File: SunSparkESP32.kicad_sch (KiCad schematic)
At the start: 50 parts, among them J1 Conn_01x02_Pin, J2 USB_C_Receptacle_USB2.0, J4 Conn_01x15_Pin, J5 Conn_01x03_Pin, J6 Conn_01x15_Pin, J7 Conn_01x01_Pin, Q1 IRLML6244TRPBF, Q2 IRLML6244TRPBF, SW1 SW_Push, SW2 SW_Push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

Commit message: Minor improvements on documentation
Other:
- note added: "Dimensioned as follows: 300µA average current, needs to be supplied for 12h (during night) U(0)=3.5V -> U(12h)=3.1V At least ~32F Powerstage must tolerate 100mA for ~200ms Current spikes 300mA for 1ms R_ESR + R_SYS + R_BAT + R_PGOOD = 0.2 + 0.48 + 0.55 + 0.02 = 1.25Ohm"
- note removed: "Dimensioned as follows: 300µA average current, needs to be supplied for 12h (during night) U(0)=3.5V -> U(12h)=3.1V At least ~32F"
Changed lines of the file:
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@@
     (effects (font (size 1.27 1.27)) (justify left bottom))
   )
-  (text "Dimensioned as follows:\n300µA average current, needs to\nbe supplied for 12h (during night)\nU(0)=3.5V -> U(12h)=3.1V\nAt least ~32F"
-    (at 106.68 52.07 0)
+  (text "Dimensioned as follows:\n300µA average current, needs to\nbe supplied for 12h (during night)\nU(0)=3.5V -> U(12h)=3.1V\nAt least ~32F\n\nPowerstage must tolerate 100mA for ~200ms\nCurrent spikes 300mA for 1ms\nR_ESR + R_SYS + R_BAT + R_PGOOD =\n0.2 + 0.48 + 0.55 + 0.02 = 1.25Ohm"
+    (at 106.68 45.72 0)
     (effects (font (size 1.27 1.27)) (justify left bottom))
   )

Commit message: Final adjustments for release preparation -Updated schematics, BOM and fabrication files -Added solder jumper so RFM96 can be powered independently
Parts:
- added JP2: SolderJumper_2_Open, Jumper:SolderJumper-2_P1.3mm_Open_RoundedPad1.0x1.5mm, symbol Jumper:SolderJumper_2_Open
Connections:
- net +BATT: now also JP2.2 (B); no longer U4.13 (3.3V)
- new net: JP2.1 (A), U4.13 (3.3V)
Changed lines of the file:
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@@
-    (stroke (width 0) (type default))
-  )
-  (wire (pts (xy 223.52 184.15) (xy 223.52 186.69))
     (stroke (width 0) (type default))
   )
@@
     (stroke (width 0) (type default))
   )
+  (wire (pts (xy 223.52 184.785) (xy 223.52 186.69))
+    (stroke (width 0) (type default))
+  )
   (wire (pts (xy 86.36 104.14) (xy 88.9 104.14))
     (stroke (width 0) (type default))
@@
   )
   (wire (pts (xy 82.55 143.51) (xy 91.44 143.51))
+    (stroke (width 0) (type default))
+  )
+  (wire (pts (xy 223.52 173.99) (xy 223.52 177.165))
     (stroke (width 0) (type default))
   )
@@
     )
   )
-  (symbol (lib_id "power:+BATT") (at 223.52 184.15 0) (unit 1)
-    (in_bom yes) (on_board yes) (dnp no) (fields_autoplaced)
-    (property "Reference" "#PWR035" (at 223.52 187.96 0)
-      (effects (font (size 1.27 1.27)) hide)
-    )
-    (property "Value" "+BATT" (at 223.52 180.34 0)
-      (effects (font (size 1.27 1.27)))
-    )
-    (property "Footprint" "" (at 223.52 184.15 0)
-      (effects (font (size 1.27 1.27)) hide)
-    )
-    (property "Datasheet" "" (at 223.52 184.15 0)
+  (symbol (lib_id "power:+BATT") (at 223.52 173.99 0) (unit 1)
+    (in_bom yes) (on_board yes) (dnp no) (fields_autoplaced)
+    (property "Reference" "#PWR035" (at 223.52 177.8 0)
+      (effects (font (size 1.27 1.27)) hide)
+    )
+    (property "Value" "+BATT" (at 223.52 170.18 0)
+      (effects (font (size 1.27 1.27)))
+    )
+    (property "Footprint" "" (at 223.52 173.99 0)
+      (effects (font (size 1.27 1.27)) hide)
+    )
+    (property "Datasheet" "" (at 223.52 173.99 0)
       (effects (font (size 1.27 1.27)) hide)
     )
@@
         )
       )
+    )
+  )
+  (symbol (lib_id "Jumper:SolderJumper_2_Open") (at 223.52 180.975 90) (unit 1)
+    (in_bom yes) (on_board yes) (dnp no) (fields_autoplaced)
+    (property "Reference" "JP2" (at 225.425 180.34 90)
+      (effects (font (size 1.27 1.27)) (justify right))
+    )
+    (property "Value" "SolderJumper_2_Open" (at 225.425 182.88 90)
+      (effects (font (size 1.27 1.27)) (justify right))
+    )
+    (property "Footprint" "Jumper:SolderJumper-2_P1.3mm_Open_RoundedPad1.0x1.5mm" (at 223.52 180.975 0)
+      (effects (font (size 1.27 1.27)) hide)
+    )
+    (property "Datasheet" "~" (at 223.52 180.975 0)
+      (effects (font (size 1.27 1.27)) hide)
+    )
+    (pin "1")
+    (pin "2")
+    (instances
+      (project "SunSparkESP32"
+        (path "/d10941bc-74a1-4d19-894b-f93374d839a2"
+          (reference "JP2") (unit 1)
+        )
+      )

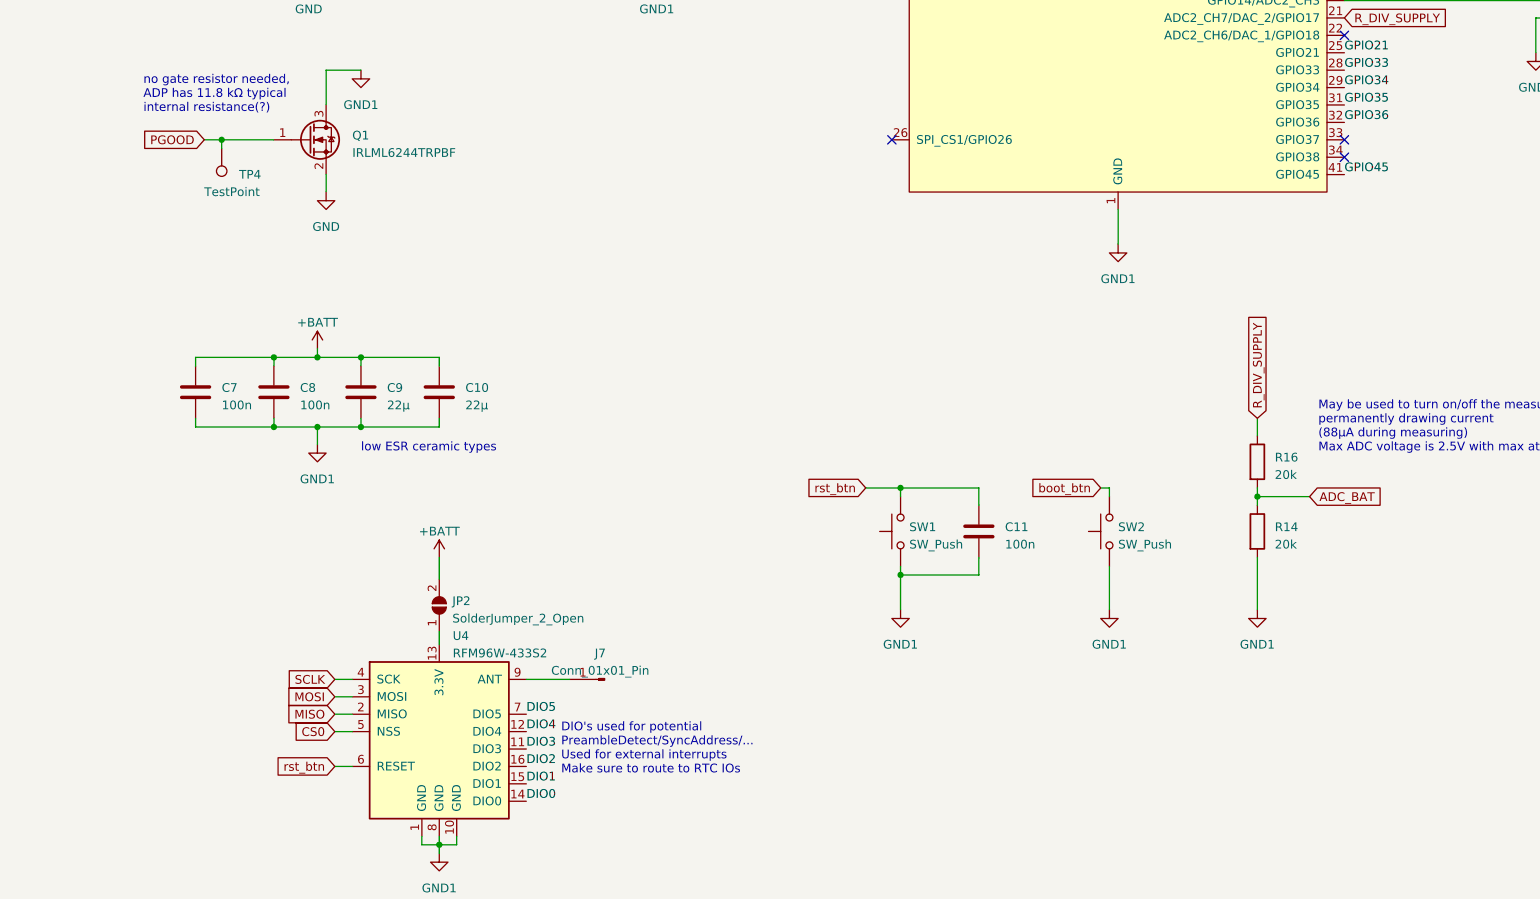
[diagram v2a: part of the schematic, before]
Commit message: connected RF96 pin to µC instead of reset button
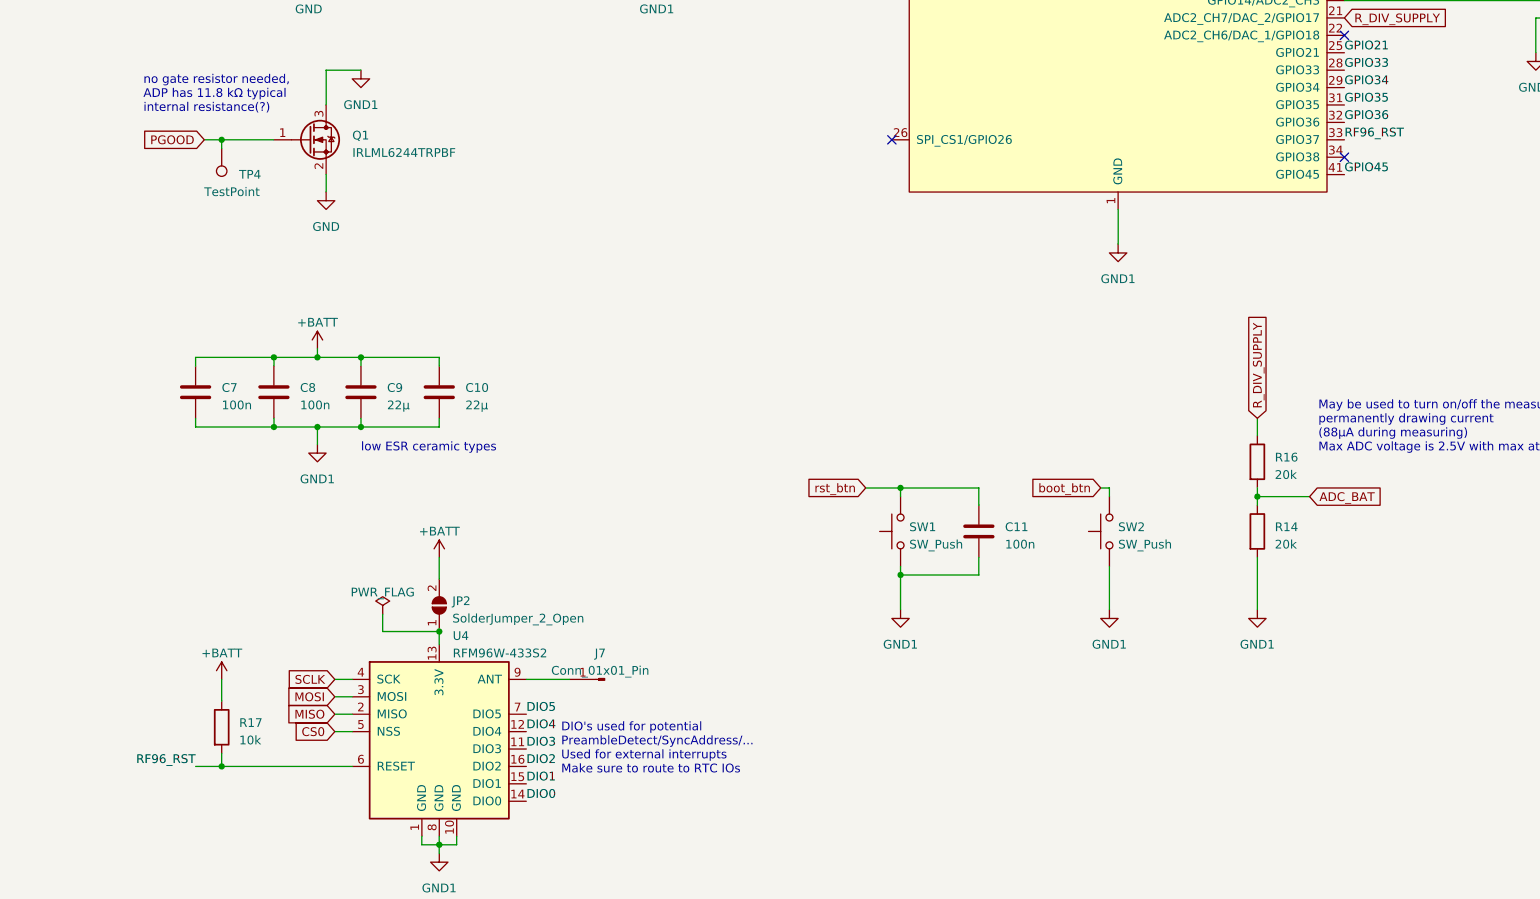
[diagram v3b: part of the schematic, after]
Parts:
- added R17: 10k, Resistor_SMD:R_0805_2012Metric_Pad1.20x1.40mm_HandSolder, symbol Device:R
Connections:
- net +BATT: now also R17.1
- net rst_btn: no longer U4.6 (RESET)
- net RF96_RST: now reaches U3.33 (GPIO37)
- net RF96_RST: now also U4.6 (RESET), R17.2
- no-connect marks 7 -> 6
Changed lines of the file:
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@@
   (junction (at 129.54 78.74) (diameter 0) (color 0 0 0 0)
   )
+  (junction (at 223.52 184.785) (diameter 0) (color 0 0 0 0)
+  )
   (junction (at 204.47 86.36) (diameter 0) (color 0 0 0 0)
   )
@@
   )
   (junction (at 157.48 74.93) (diameter 0) (color 0 0 0 0)
+  )
+  (junction (at 191.77 204.47) (diameter 0) (color 0 0 0 0)
   )
   (junction (at 199.39 154.94) (diameter 0) (color 0 0 0 0)
@@
   (no_connect (at 289.56 113.03))
   (no_connect (at 289.56 69.85))
-  (no_connect (at 355.6 113.03))
   (wire (pts (xy 321.31 175.26) (xy 321.31 181.61))
     (stroke (width 0) (type default))
@@
     (stroke (width 0) (type default))
   )
-  (wire (pts (xy 208.28 204.47) (xy 210.82 204.47))
+  (wire (pts (xy 191.77 204.47) (xy 210.82 204.47))
     (stroke (width 0) (type default))
   )
@@
     (stroke (width 0) (type default))
   )
+  (wire (pts (xy 187.96 204.47) (xy 191.77 204.47))
+    (stroke (width 0) (type default))
+  )
   (wire (pts (xy 187.96 153.67) (xy 187.96 154.94))
     (stroke (width 0) (type default))
@@
     (stroke (width 0) (type default))
   )
+  (wire (pts (xy 191.77 204.47) (xy 191.77 202.565))
+    (stroke (width 0) (type default))
+  )
   (wire (pts (xy 199.39 154.94) (xy 199.39 153.67))
     (stroke (width 0) (type default))
@@
     (stroke (width 0) (type default))
   )
+  (wire (pts (xy 191.77 191.77) (xy 191.77 194.945))
+    (stroke (width 0) (type default))
+  )
   (wire (pts (xy 208.28 199.39) (xy 210.82 199.39))
     (stroke (width 0) (type default))
@@
     (stroke (width 0) (type default))
   )
+  (wire (pts (xy 215.265 184.785) (xy 223.52 184.785))
+    (stroke (width 0) (type default))
+  )
   (wire (pts (xy 302.26 166.37) (xy 302.26 163.83))
     (stroke (width 0) (type default))
@@
   )
   (wire (pts (xy 129.54 78.74) (xy 129.54 80.01))
+    (stroke (width 0) (type default))
+  )
+  (wire (pts (xy 215.265 182.245) (xy 215.265 184.785))
     (stroke (width 0) (type default))
   )
@@
   (label "GPIO45" (at 254 77.47 0) (fields_autoplaced)
     (effects (font (size 1.27 1.27)) (justify left bottom))
+  )
+  (label "RF96_RST" (at 355.6 113.03 0) (fields_autoplaced)
+    (effects (font (size 1.27 1.27)) (justify left bottom))
+  )
+  (label "RF96_RST" (at 187.96 204.47 180) (fields_autoplaced)
+    (effects (font (size 1.27 1.27)) (justify right bottom))
   )
   (label "DIO3" (at 236.22 201.93 0) (fields_autoplaced)
@@
     (property "Intersheetrefs" "${INTERSHEET_REFS}" (at 342.9 137.3989 90)
       (effects (font (size 1.27 1.27)) (justify left) hide)
-    )
-  )
-  (global_label "rst_btn" (shape input) (at 208.28 204.47 180) (fields_autoplaced)
-    (effects (font (size 1.27 1.27)) (justify right))
-    (property "Intersheetrefs" "${INTERSHEET_REFS}" (at 198.8429 204.47 0)
-      (effects (font (size 1.27 1.27)) (justify right) hide)
     )
   )
@@
     )
   )
+  (symbol (lib_id "power:PWR_FLAG") (at 215.265 182.245 0) (unit 1)
+    (in_bom yes) (on_board yes) (dnp no) (fields_autoplaced)
+    (property "Reference" "#FLG04" (at 215.265 180.34 0)
+      (effects (font (size 1.27 1.27)) hide)
+    )
+    (property "Value" "PWR_FLAG" (at 215.265 179.07 0)
+      (effects (font (size 1.27 1.27)))
+    )
+    (property "Footprint" "" (at 215.265 182.245 0)
+      (effects (font (size 1.27 1.27)) hide)
+    )
+    (property "Datasheet" "~" (at 215.265 182.245 0)
+      (effects (font (size 1.27 1.27)) hide)
+    )
+    (pin "1")
+    (instances
+      (project "SunSparkESP32"
+        (path "/d10941bc-74a1-4d19-894b-f93374d839a2"
+          (reference "#FLG04") (unit 1)
+        )
+      )
+    )
+  )
   (symbol (lib_id "Device:L") (at 67.31 74.93 90) (unit 1)
     (in_bom yes) (on_board yes) (dnp no) (fields_autoplaced)
@@
     )
   )
+  (symbol (lib_id "Device:R") (at 191.77 198.755 0) (unit 1)
+    (in_bom yes) (on_board yes) (dnp no) (fields_autoplaced)
+    (property "Reference" "R17" (at 194.31 198.12 0)
+      (effects (font (size 1.27 1.27)) (justify left))
+    )
+    (property "Value" "10k" (at 194.31 200.66 0)
+      (effects (font (size 1.27 1.27)) (justify left))
+    )
+    (property "Footprint" "Resistor_SMD:R_0805_2012Metric_Pad1.20x1.40mm_HandSolder" (at 189.992 198.755 90)
+      (effects (font (size 1.27 1.27)) hide)
+    )
+    (property "Datasheet" "~" (at 191.77 198.755 0)
+      (effects (font (size 1.27 1.27)) hide)
+    )
+    (pin "1")
+    (pin "2")
+    (instances
+      (project "SunSparkESP32"
+        (path "/d10941bc-74a1-4d19-894b-f93374d839a2"
+          (reference "R17") (unit 1)
+        )
+      )
+    )
+  )
   (symbol (lib_id "power:+BATT") (at 322.58 31.75 0) (unit 1)
     (in_bom yes) (on_board yes) (dnp no) (fields_autoplaced)
@@
         )
       )
+    )
+  )
+  (symbol (lib_id "power:+BATT") (at 191.77 191.77 0) (unit 1)
+    (in_bom yes) (on_board yes) (dnp no) (fields_autoplaced)
+    (property "Reference" "#PWR028" (at 191.77 195.58 0)
+      (effects (font (size 1.27 1.27)) hide)
+    )
+    (property "Value" "+BATT" (at 191.77 187.96 0)
+      (effects (font (size 1.27 1.27)))
+    )
+    (property "Footprint" "" (at 191.77 191.77 0)
+      (effects (font (size 1.27 1.27)) hide)
+    )
+    (property "Datasheet" "" (at 191.77 191.77 0)
+      (effects (font (size 1.27 1.27)) hide)
+    )
+    (pin "1")
+    (instances
+      (project "SunSparkESP32"
+        (path "/d10941bc-74a1-4d19-894b-f93374d839a2"
+          (reference "#PWR028") (unit 1)
+        )
+      )
